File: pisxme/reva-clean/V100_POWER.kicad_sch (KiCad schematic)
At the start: 0 parts

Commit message: add native Phase 3 contract connectivity
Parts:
- added X: V100_POWER_Contract
- added XV1: V100_POWER_Contract, symbol PiSXMeRevAClean:V100_POWER_Contract
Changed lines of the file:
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@@
 (kicad_sch (version 20230409) (generator "eeschema")
   (paper "A4")
+    (symbol "PiSXMeRevAClean:V100_POWER_Contract"
+      (pin_names (offset 1.0))
+      (exclude_from_sim no)
+      (in_bom yes)
+      (on_board yes)
+      (property "Reference" "X"
+        (at 0 -5.539999999999999 0)
+        (effects (font (size 1.27 1.27))))
+      (property "Value" "V100_POWER_Contract"
+        (at 0 5.539999999999999 0)
+        (effects (font (size 1.27 1.27))))
+      (property "Footprint" ""
+        (at 0 0 0)
+        (effects (font (size 1.27 1.27)) (hide yes)))
+      (property "Datasheet" "~"
+        (at 0 0 0)
+        (effects (font (size 1.27 1.27)) (hide yes)))
+      (symbol "V100_POWER_Contract_1_1"
+        (rectangle (start -1.27 -4.27) (end 1.27 4.27)
+          (stroke (width 0.254) (type default)) (fill (type background)))
+        (pin passive line
+          (at -5.08 0 0)
+          (length 3.81)
+          (name "V100_POWER_12V" (effects (font (size 1.27 1.27))))
+          (number "1" (effects (font (size 1.27 1.27)))))
+        (pin passive line
+          (at -5.08 3 0)
+          (length 3.81)
+          (name "V100_GND" (effects (font (size 1.27 1.27))))
+          (number "2" (effects (font (size 1.27 1.27)))))
+        (pin passive line
+          (at -5.08 6 0)
+          (length 3.81)
+          (name "V100_THERMAL" (effects (font (size 1.27 1.27))))
+          (number "3" (effects (font (size 1.27 1.27)))))
+      )
+    )
   (hierarchical_label "V100_POWER_12V"
     (shape bidirectional)
@@
     (effects (font (size 1.27 1.27)) (justify left))
 )
-  (sheet_instances (path "/3" (page "3")))
+  (wire
+    (pts (xy 5 10) (xy 19.92 10))
+    (stroke (width 0) (type default))
 )
+  (wire
+    (pts (xy 5 13) (xy 19.92 13))
+    (stroke (width 0) (type default))
+)
+  (wire
+    (pts (xy 5 16) (xy 19.92 16))
+    (stroke (width 0) (type default))
+)
+  (symbol
+    (lib_id "PiSXMeRevAClean:V100_POWER_Contract")
+    (at 25 10 0)
+    (unit 1)
+    (exclude_from_sim no)
+    (in_bom no)
+    (on_board no)
+    (dnp no)
+    (property "Reference" "XV1"
+      (at 25 5 0)
+      (effects (font (size 1.27 1.27))))
+    (property "Value" "V100_POWER_Contract"
+      (at 25 18 0)
+      (effects (font (size 1.27 1.27))))
+    (property "Footprint" ""
+      (at 25 10 0)
+      (effects (font (size 1.27 1.27)) (hide yes)))
+    (property "Datasheet" "~"
+      (at 25 10 0)
+      (effects (font (size 1.27 1.27)) (hide yes)))
+    (pin "1")
+    (pin "2")
+    (pin "3")
+    (instances (project "PiSXMe_RevA_Clean"
+      (path "/30000000-0000-0000-0000-000000000000/10000000-0000-0000-0000-000000000003" (reference "XV1" ) (unit 1))))
+  )
+  (sheet_instances (path "/30000000-0000-0000-0000-000000000000/10000000-0000-0000-0000-000000000003" (page "3")))
+)

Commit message: close native Phase 3 hierarchy association
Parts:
- removed X: V100_POWER_Contract
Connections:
- net V100_GND: now also XV1.2 (V100_GND)
- net V100_POWER_12V: now also XV1.1 (V100_POWER_12V)
- net V100_THERMAL: now also XV1.3 (V100_THERMAL)
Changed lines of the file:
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@@
 (kicad_sch (version 20230409) (generator "eeschema")
   (paper "A4")
-    (symbol "PiSXMeRevAClean:V100_POWER_Contract"
-      (pin_names (offset 1.0))
-      (exclude_from_sim no)
-      (in_bom yes)
-      (on_board yes)
-      (property "Reference" "X"
-        (at 0 -5.539999999999999 0)
-        (effects (font (size 1.27 1.27))))
-      (property "Value" "V100_POWER_Contract"
-        (at 0 5.539999999999999 0)
-        (effects (font (size 1.27 1.27))))
-      (property "Footprint" ""
-        (at 0 0 0)
-        (effects (font (size 1.27 1.27)) (hide yes)))
-      (property "Datasheet" "~"
-        (at 0 0 0)
-        (effects (font (size 1.27 1.27)) (hide yes)))
-      (symbol "V100_POWER_Contract_1_1"
-        (rectangle (start -1.27 -4.27) (end 1.27 4.27)
-          (stroke (width 0.254) (type default)) (fill (type background)))
-        (pin passive line
-          (at -5.08 0 0)
-          (length 3.81)
-          (name "V100_POWER_12V" (effects (font (size 1.27 1.27))))
-          (number "1" (effects (font (size 1.27 1.27)))))
-        (pin passive line
-          (at -5.08 3 0)
-          (length 3.81)
-          (name "V100_GND" (effects (font (size 1.27 1.27))))
-          (number "2" (effects (font (size 1.27 1.27)))))
-        (pin passive line
-          (at -5.08 6 0)
-          (length 3.81)
-          (name "V100_THERMAL" (effects (font (size 1.27 1.27))))
-          (number "3" (effects (font (size 1.27 1.27)))))
-      )
-    )
   (hierarchical_label "V100_POWER_12V"
     (shape bidirectional)
-    (at 5 10 0)
-    (effects (font (size 1.27 1.27)) (justify left))
+    (at 5 10 180)
+    (effects (font (size 1.27 1.27)) (justify right))
 )
   (hierarchical_label "V100_GND"
     (shape bidirectional)
-    (at 5 13 0)
-    (effects (font (size 1.27 1.27)) (justify left))
+    (at 5 13 180)
+    (effects (font (size 1.27 1.27)) (justify right))
 )
   (hierarchical_label "V100_THERMAL"
     (shape bidirectional)
-    (at 5 16 0)
-    (effects (font (size 1.27 1.27)) (justify left))
+    (at 5 16 180)
+    (effects (font (size 1.27 1.27)) (justify right))
 )
   (wire

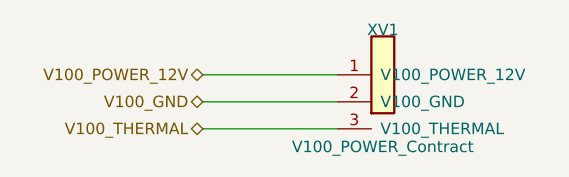
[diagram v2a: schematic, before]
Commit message: stabilize Phase 3 hierarchy netlist references
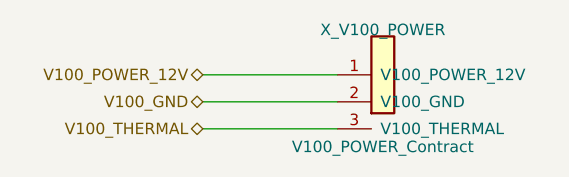
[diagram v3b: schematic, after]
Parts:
- renumbered XV1 to X_V100_POWER
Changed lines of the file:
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@@
     (on_board no)
     (dnp no)
-    (property "Reference" "XV1"
+    (property "Reference" "X_V100_POWER"
       (at 25 5 0)
       (effects (font (size 1.27 1.27))))
@@
     (pin "3")
     (instances (project "PiSXMe_RevA_Clean"
-      (path "/30000000-0000-0000-0000-000000000000/10000000-0000-0000-0000-000000000003" (reference "XV1" ) (unit 1))))
+      (path "/30000000-0000-0000-0000-000000000000/10000000-0000-0000-0000-000000000003" (reference "X_V100_POWER" ) (unit 1))))
   )
   (sheet_instances (path "/30000000-0000-0000-0000-000000000000/10000000-0000-0000-0000-000000000003" (page "3")))

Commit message: fix KiCad annotation and netlist export
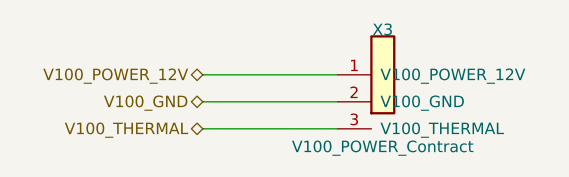
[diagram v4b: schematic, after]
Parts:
- renumbered X_V100_POWER to X3
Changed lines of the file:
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@@
     (on_board no)
     (dnp no)
-    (property "Reference" "X_V100_POWER"
+    (property "Reference" "X3"
       (at 25 5 0)
       (effects (font (size 1.27 1.27))))
@@
     (pin "3")
     (instances (project "PiSXMe_RevA_Clean"
-      (path "/30000000-0000-0000-0000-000000000000/10000000-0000-0000-0000-000000000003" (reference "X_V100_POWER" ) (unit 1))))
+      (path "/30000000-0000-0000-0000-000000000000/10000000-0000-0000-0000-000000000003" (reference "X3" ) (unit 1))))
   )
   (sheet_instances (path "/30000000-0000-0000-0000-000000000000/10000000-0000-0000-0000-000000000003" (page "3")))

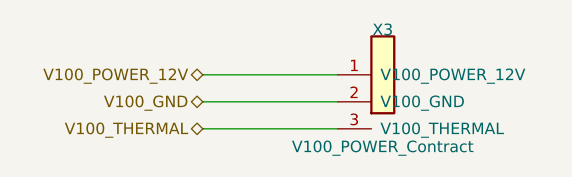
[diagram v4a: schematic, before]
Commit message: phase24: promote identity-preserving hierarchy repair
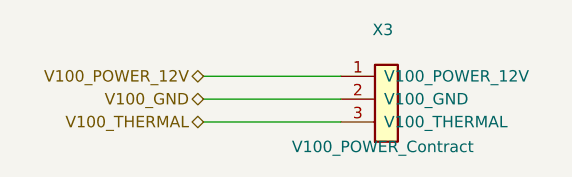
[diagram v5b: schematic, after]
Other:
- moved on the sheet: X3
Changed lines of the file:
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@@
   (hierarchical_label "V100_POWER_12V"
     (shape bidirectional)
-    (at 5 10 180)
+    (at 5.08 10.16 180)
     (effects (font (size 1.27 1.27)) (justify right))
 )
   (hierarchical_label "V100_GND"
     (shape bidirectional)
-    (at 5 13 180)
+    (at 5.08 12.7 180)
     (effects (font (size 1.27 1.27)) (justify right))
 )
   (hierarchical_label "V100_THERMAL"
     (shape bidirectional)
-    (at 5 16 180)
+    (at 5.08 15.24 180)
     (effects (font (size 1.27 1.27)) (justify right))
 )
   (wire
-    (pts (xy 5 10) (xy 19.92 10))
+    (pts (xy 5.08 10.16) (xy 20.32 10.16))
     (stroke (width 0) (type default))
 )
   (wire
-    (pts (xy 5 13) (xy 19.92 13))
+    (pts (xy 5.08 12.7) (xy 20.32 12.7))
     (stroke (width 0) (type default))
 )
   (wire
-    (pts (xy 5 16) (xy 19.92 16))
+    (pts (xy 5.08 15.24) (xy 20.32 15.24))
     (stroke (width 0) (type default))
 )
   (symbol
     (lib_id "PiSXMeRevAClean:V100_POWER_Contract")
-    (at 25 10 0)
+    (at 25.4 10.16 0)
     (unit 1)
     (exclude_from_sim no)
@@
       (effects (font (size 1.27 1.27))))
     (property "Footprint" ""
-      (at 25 10 0)
+      (at 25.4 10.16 0)
       (effects (font (size 1.27 1.27)) (hide yes)))
     (property "Datasheet" "~"
-      (at 25 10 0)
+      (at 25.4 10.16 0)
       (effects (font (size 1.27 1.27)) (hide yes)))
-    (pin "1")
+        (pin "1")
     (pin "2")
     (pin "3")
